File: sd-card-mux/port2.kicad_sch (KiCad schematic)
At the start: 10 parts, among them J201 47309-2285, U201 74LVC1G3157, U202 74LVC1G3157, U203 74LVC1G3157, U204 74LVC1G3157, U205 74LVC1G3157, U206 74LVC1G3157

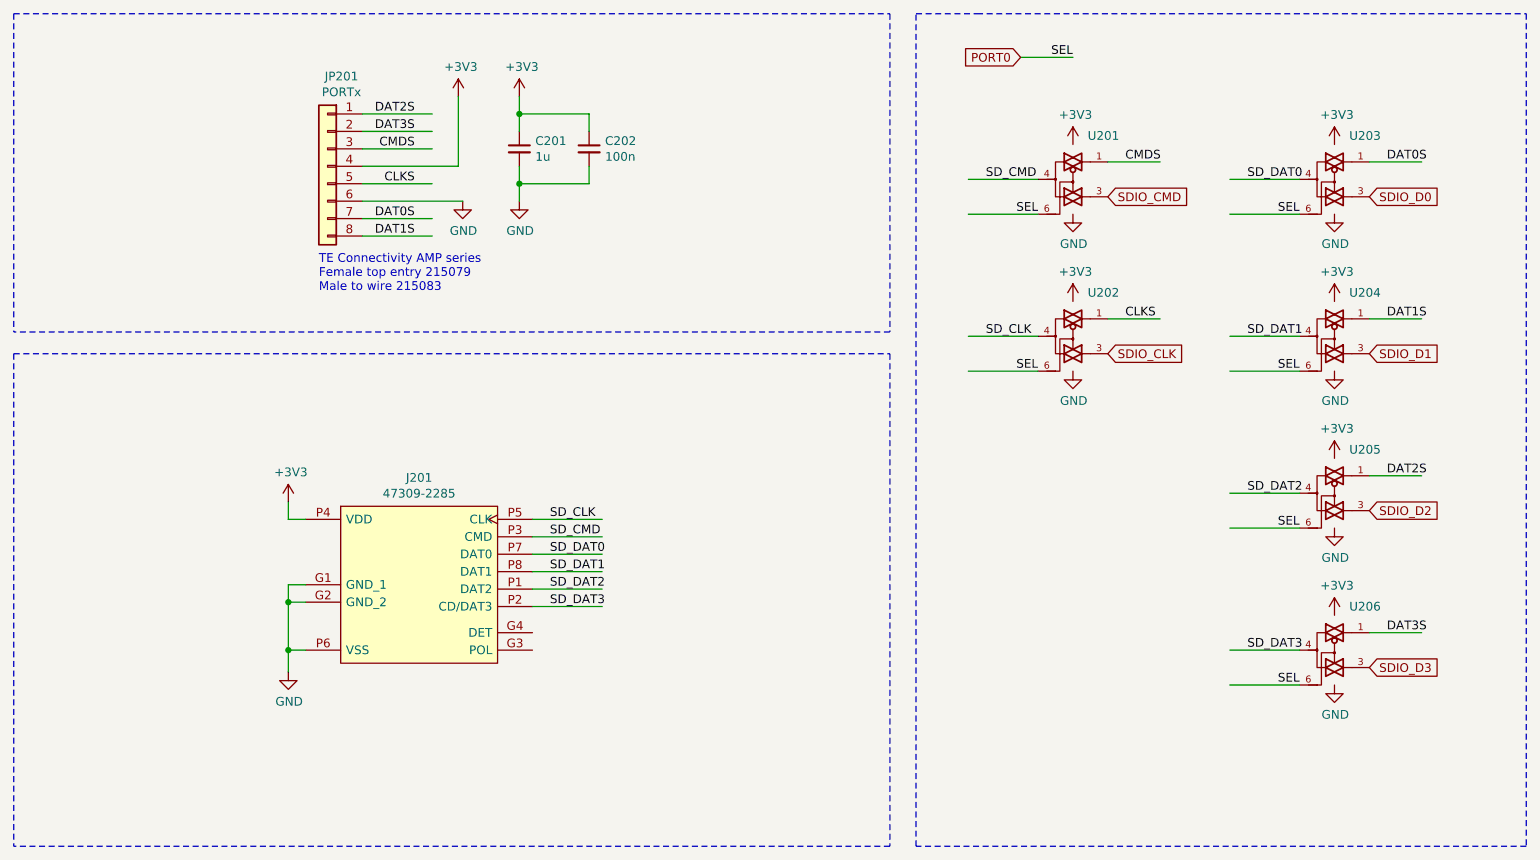
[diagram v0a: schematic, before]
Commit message: Added MCP23008 alternative
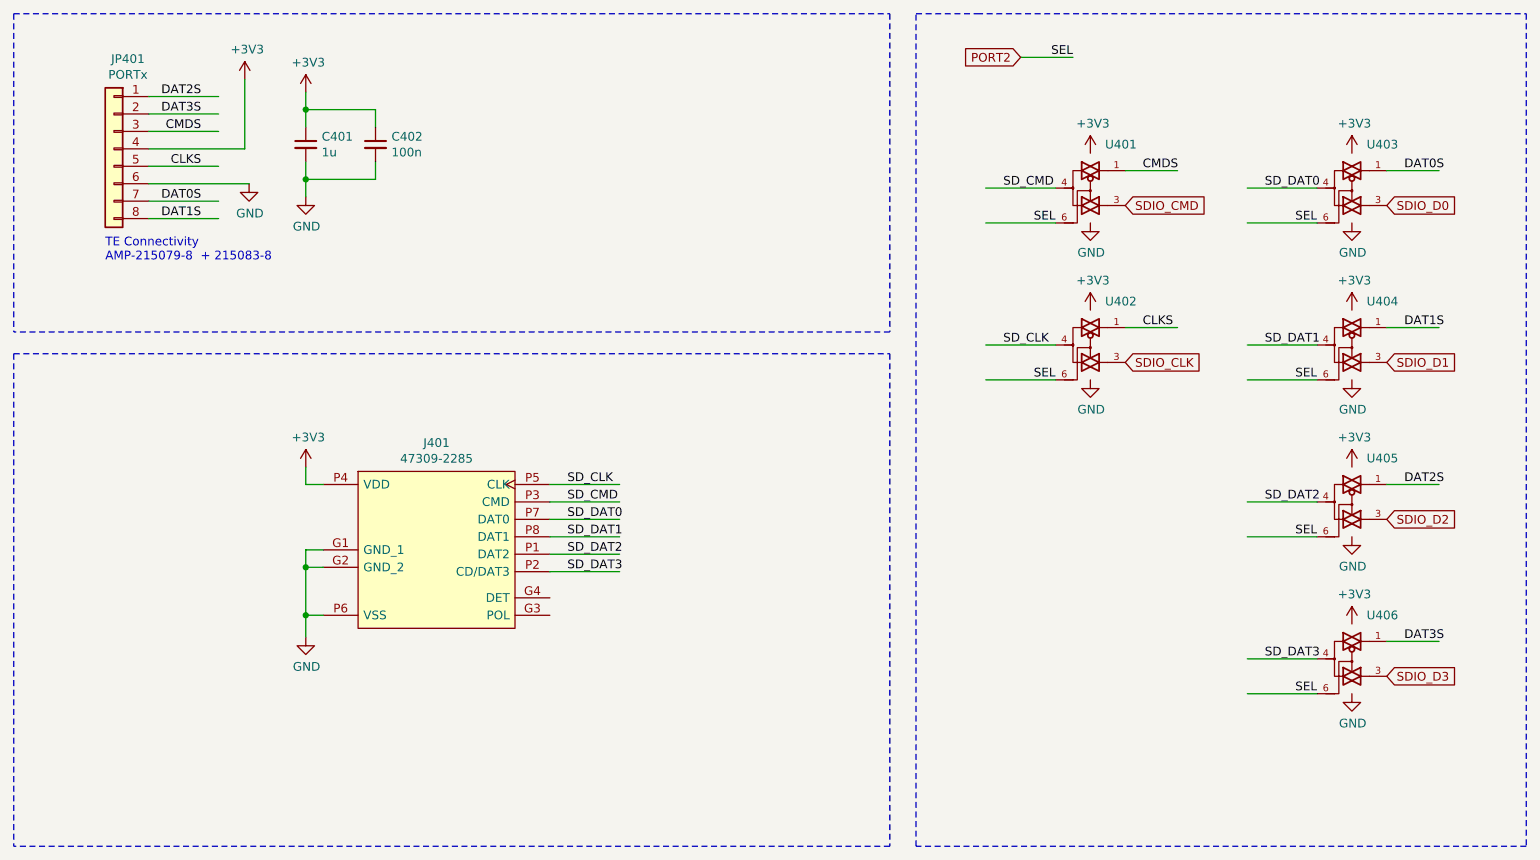
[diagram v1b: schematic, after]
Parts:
- removed C201: 1u, Capacitor_SMD:C_0402_1005Metric, symbol Device:C_Small
- removed C202: 100n, Capacitor_SMD:C_0402_1005Metric, symbol Device:C_Small
- removed J201: 47309-2285, footprints:47309-2285, symbol 47309-2285:47309-2285
- removed JP201: PORTx, Connector_JST:JST_PH_S8B-PH-K_1x08_P2.00mm_Horizontal, symbol Connector_Generic:Conn_01x08
- removed U201, U202, U203, U204, U205, U206: 74LVC1G3157, Package_TO_SOT_SMD:SOT-363_SC-70-6, symbol 74LVC1G3157:74LVC1G3157
- added C401: 1u, Capacitor_SMD:C_0402_1005Metric, symbol Device:C_Small
- added C402: 100n, Capacitor_SMD:C_0402_1005Metric, symbol Device:C_Small
- added J401: 47309-2285, footprints:47309-2285, symbol 47309-2285:47309-2285
- added JP401: PORTx, Connector_JST:JST_PH_S8B-PH-K_1x08_P2.00mm_Horizontal, symbol Connector_Generic:Conn_01x08
- added U401, U402, U403, U404, U405, U406: 74LVC1G3157, Package_TO_SOT_SMD:SOT-363_SC-70-6, symbol 74LVC1G3157:74LVC1G3157
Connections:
- net +3V3: now also C401.1, C402.1, J401.P4 (VDD), JP401.4 (Pin_4), U401.5 (VCC), U402.5 (VCC), U403.5 (VCC), U404.5 (VCC), U405.5 (VCC), U406.5 (VCC)
- net CLKS: now also JP401.5 (Pin_5), U402.1
- net CMDS: now also JP401.3 (Pin_3), U401.1
- net DAT0S: now also JP401.7 (Pin_7), U403.1
- net DAT1S: now also JP401.8 (Pin_8), U404.1
- net DAT2S: now also JP401.1 (Pin_1), U405.1
- net DAT3S: now also JP401.2 (Pin_2), U406.1
- net GND: now also C401.2, C402.2, J401.G1 (GND_1), J401.G2 (GND_2), J401.P6 (VSS), JP401.6 (Pin_6), U401.2 (GND), U402.2 (GND), U403.2 (GND), U404.2 (GND), U405.2 (GND), U406.2 (GND)
- net SDIO_CLK: now also U402.3
- net SDIO_CMD: now also U401.3
- net SDIO_D0: now also U403.3
- net SDIO_D1: now also U404.3
- net SDIO_D2: now also U405.3
- net SDIO_D3: now also U406.3
- net SD_CLK: now also J401.P5 (CLK), U402.4
- net SD_CMD: now also J401.P3 (CMD), U401.4
- net SD_DAT0: now also J401.P7 (DAT0), U403.4
- net SD_DAT1: now also J401.P8 (DAT1), U404.4
- net SD_DAT2: now also J401.P1 (DAT2), U405.4
- net SD_DAT3: now also J401.P2 (CD/DAT3), U406.4
- new net PORT2: U401.6, U402.6, U403.6, U404.6, U405.6, U406.6
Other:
- note added: "TE Connectivity AMP-215079-8 + 215083-8"
- note removed: "TE Connectivity AMP series Female top entry 215079 Male to wire 215083"

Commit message: Addedd missing upload port
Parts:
- C401: LCSC Part# (none) -> C52923
- C402: LCSC Part# (none) -> C1525
- JP401: footprint Connector_JST:JST_PH_S8B-PH-K_1x08_P2.00mm_Horizontal -> footprints:ConnectorMicromatch-8
- U401, U402, U403, U404, U405, U406: LCSC Part# (none) -> C38663
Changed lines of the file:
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@@
+      (effects (font (size 1.27 1.27)) hide)
+    )
+    (property "LCSC Part#" "C52923" (id 4) (at 63.5 38.1 0)
       (effects (font (size 1.27 1.27)) hide)
     )
@@
       (effects (font (size 1.27 1.27)) hide)
     )
+    (property "LCSC Part#" "C1525" (id 4) (at 73.66 38.1 0)
+      (effects (font (size 1.27 1.27)) hide)
+    )
   )
   (symbol (lib_name "74LVC1G3157:74LVC1G3157_2") (lib_id "74LVC1G3157:74LVC1G3157") (at 177.8 44.45 0) (unit 1)
@@
     )
     (property "Datasheet" "https://www.ti.com/lit/ds/symlink/sn74lvc1g3157.pdf" (id 3) (at 177.8 44.45 0)
+      (effects (font (size 1.27 1.27)) hide)
+    )
+    (property "LCSC Part#" " C38663" (id 4) (at 177.8 44.45 0)
       (effects (font (size 1.27 1.27)) hide)
     )
@@
       (effects (font (size 1.27 1.27)) hide)
     )
+    (property "LCSC Part#" " C38663" (id 4) (at 177.8 67.31 0)
+      (effects (font (size 1.27 1.27)) hide)
+    )
   )
   (symbol (lib_id "74LVC1G3157:74LVC1G3157") (at 215.9 44.45 0) (unit 1)
@@
     )
     (property "Datasheet" "https://www.ti.com/lit/ds/symlink/sn74lvc1g3157.pdf" (id 3) (at 215.9 44.45 0)
+      (effects (font (size 1.27 1.27)) hide)
+    )
+    (property "LCSC Part#" " C38663" (id 4) (at 215.9 44.45 0)
       (effects (font (size 1.27 1.27)) hide)
     )
@@
       (effects (font (size 1.27 1.27)) hide)
     )
+    (property "LCSC Part#" " C38663" (id 4) (at 215.9 67.31 0)
+      (effects (font (size 1.27 1.27)) hide)
+    )
   )
   (symbol (lib_id "74LVC1G3157:74LVC1G3157") (at 215.9 90.17 0) (unit 1)
@@
     )
     (property "Datasheet" "https://www.ti.com/lit/ds/symlink/sn74lvc1g3157.pdf" (id 3) (at 215.9 90.17 0)
+      (effects (font (size 1.27 1.27)) hide)
+    )
+    (property "LCSC Part#" " C38663" (id 4) (at 215.9 90.17 0)
       (effects (font (size 1.27 1.27)) hide)
     )
@@
       (effects (font (size 1.27 1.27)) hide)
     )
+    (property "LCSC Part#" " C38663" (id 4) (at 215.9 113.03 0)
+      (effects (font (size 1.27 1.27)) hide)
+    )
   )
   (symbol (lib_id "Connector_Generic:Conn_01x08") (at 35.56 38.735 0) (mirror y) (unit 1)
@@
     (property "Reference" "JP401" (id 0) (at 37.592 25.635 0))
     (property "Value" "PORTx" (id 1) (at 37.592 27.9335 0))
-    (property "Footprint" "Connector_JST:JST_PH_S8B-PH-K_1x08_P2.00mm_Horizontal" (id 2) (at 35.56 38.735 0)
+    (property "Footprint" "footprints:ConnectorMicromatch-8" (id 2) (at 35.56 38.735 0)
       (effects (font (size 1.27 1.27)) hide)
     )

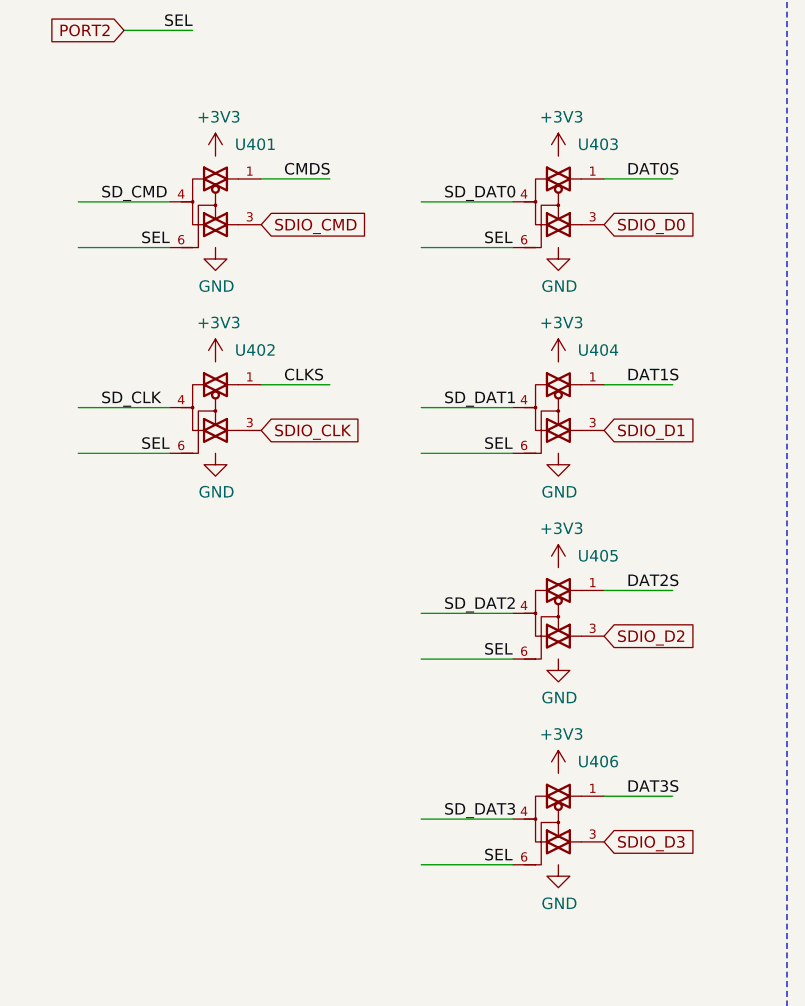
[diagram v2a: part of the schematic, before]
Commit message: Correction of inverted pins
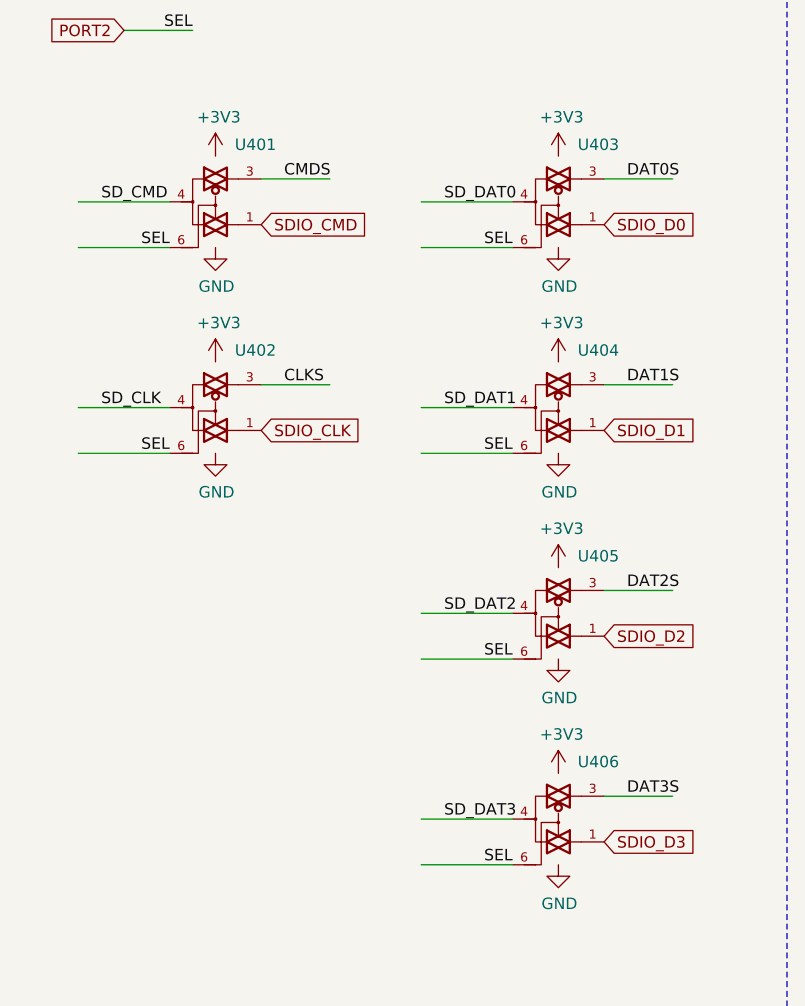
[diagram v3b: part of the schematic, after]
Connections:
- net CLKS: now also U402.3; no longer U402.1
- net CMDS: now also U401.3; no longer U401.1
- net DAT0S: now also U403.3; no longer U403.1
- net DAT1S: now also U404.3; no longer U404.1
- net DAT2S: now also U405.3; no longer U405.1
- net DAT3S: now also U406.3; no longer U406.1
- net SDIO_CLK: now also U402.1; no longer U402.3
- net SDIO_CMD: now also U401.1; no longer U401.3
- net SDIO_D0: now also U403.1; no longer U403.3
- net SDIO_D1: now also U404.1; no longer U404.3
- net SDIO_D2: now also U405.1; no longer U405.3
- net SDIO_D3: now also U406.1; no longer U406.3
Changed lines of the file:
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@@
 (kicad_sch (version 20200608) (host eeschema "(5.99.0-1973-g8c57821e9)")
-  (page 1 9)
+  (page 4 9)
   (paper "A4")
   (junction (at 63.5 33.02))
@@
     )
   )
-  (symbol (lib_id "74LVC1G3157:74LVC1G3157") (at 177.8 67.31 0) (unit 1)
+  (symbol (lib_name "74LVC1G3157:74LVC1G3157_1") (lib_id "74LVC1G3157:74LVC1G3157") (at 177.8 67.31 0) (unit 1)
     (in_bom yes) (on_board yes)
     (property "Reference" "U402" (id 0) (at 182.245 60.96 0))
@@
     )
   )
-  (symbol (lib_id "74LVC1G3157:74LVC1G3157") (at 215.9 44.45 0) (unit 1)
+  (symbol (lib_name "74LVC1G3157:74LVC1G3157_3") (lib_id "74LVC1G3157:74LVC1G3157") (at 215.9 44.45 0) (unit 1)
     (in_bom yes) (on_board yes)
     (property "Reference" "U403" (id 0) (at 220.345 38.1 0))
@@
     )
   )
-  (symbol (lib_id "74LVC1G3157:74LVC1G3157") (at 215.9 67.31 0) (unit 1)
+  (symbol (lib_name "74LVC1G3157:74LVC1G3157_4") (lib_id "74LVC1G3157:74LVC1G3157") (at 215.9 67.31 0) (unit 1)
     (in_bom yes) (on_board yes)
     (property "Reference" "U404" (id 0) (at 220.345 60.96 0))
@@
     )
   )
-  (symbol (lib_id "74LVC1G3157:74LVC1G3157") (at 215.9 90.17 0) (unit 1)
+  (symbol (lib_name "74LVC1G3157:74LVC1G3157_5") (lib_id "74LVC1G3157:74LVC1G3157") (at 215.9 90.17 0) (unit 1)
     (in_bom yes) (on_board yes)
     (property "Reference" "U405" (id 0) (at 220.345 83.82 0))

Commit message: Removal of host port and preparation for manufacturing
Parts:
- J401: Mechanical (none) -> T
- JP401: Mechanical (none) -> T; TME Part# (none) -> MM2x5
- U401, U402, U403, U404, U405, U406: LCSC Part# C38663 -> C265126; Rotation (none) -> 0
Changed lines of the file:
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@@
       (effects (font (size 1.27 1.27)) hide)
     )
-    (property "LCSC Part#" " C38663" (id 4) (at 177.8 44.45 0)
+    (property "LCSC Part#" "C265126" (id 4) (at 177.8 44.45 0)
+      (effects (font (size 1.27 1.27)) hide)
+    )
+    (property "Rotation" "0" (id 4) (at 177.8 44.45 0)
       (effects (font (size 1.27 1.27)) hide)
     )
@@
       (effects (font (size 1.27 1.27)) hide)
     )
-    (property "LCSC Part#" " C38663" (id 4) (at 177.8 67.31 0)
+    (property "LCSC Part#" "C265126" (id 4) (at 177.8 67.31 0)
+      (effects (font (size 1.27 1.27)) hide)
+    )
+    (property "Rotation" "0" (id 4) (at 177.8 67.31 0)
       (effects (font (size 1.27 1.27)) hide)
     )
@@
       (effects (font (size 1.27 1.27)) hide)
     )
-    (property "LCSC Part#" " C38663" (id 4) (at 215.9 44.45 0)
+    (property "LCSC Part#" "C265126" (id 4) (at 215.9 44.45 0)
+      (effects (font (size 1.27 1.27)) hide)
+    )
+    (property "Rotation" "0" (id 4) (at 215.9 44.45 0)
       (effects (font (size 1.27 1.27)) hide)
     )
@@
       (effects (font (size 1.27 1.27)) hide)
     )
-    (property "LCSC Part#" " C38663" (id 4) (at 215.9 67.31 0)
+    (property "LCSC Part#" "C265126" (id 4) (at 215.9 67.31 0)
+      (effects (font (size 1.27 1.27)) hide)
+    )
+    (property "Rotation" "0" (id 4) (at 215.9 67.31 0)
       (effects (font (size 1.27 1.27)) hide)
     )
@@
       (effects (font (size 1.27 1.27)) hide)
     )
-    (property "LCSC Part#" " C38663" (id 4) (at 215.9 90.17 0)
+    (property "LCSC Part#" "C265126" (id 4) (at 215.9 90.17 0)
+      (effects (font (size 1.27 1.27)) hide)
+    )
+    (property "Rotation" "0" (id 4) (at 215.9 90.17 0)
       (effects (font (size 1.27 1.27)) hide)
     )
@@
       (effects (font (size 1.27 1.27)) hide)
     )
-    (property "LCSC Part#" " C38663" (id 4) (at 215.9 113.03 0)
+    (property "LCSC Part#" "C265126" (id 4) (at 215.9 113.03 0)
+      (effects (font (size 1.27 1.27)) hide)
+    )
+    (property "Rotation" "0" (id 4) (at 215.9 113.03 0)
       (effects (font (size 1.27 1.27)) hide)
     )
@@
     )
     (property "Datasheet" "~" (id 3) (at 35.56 38.735 0)
+      (effects (font (size 1.27 1.27)) hide)
+    )
+    (property "TME Part#" "MM2x5" (id 4) (at 35.56 38.735 0)
+      (effects (font (size 1.27 1.27)) hide)
+    )
+    (property "Mechanical" "T" (id 4) (at 35.56 38.735 0)
       (effects (font (size 1.27 1.27)) hide)
     )
@@
       (effects (font (size 1.27 1.27)) (justify left) hide)
     )
+    (property "Mechanical" "T" (id 4) (at 66.04 88.265 0)
+      (effects (font (size 1.27 1.27)) hide)
+    )
   )
